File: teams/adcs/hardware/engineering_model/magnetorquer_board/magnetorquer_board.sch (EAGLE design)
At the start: 36 parts

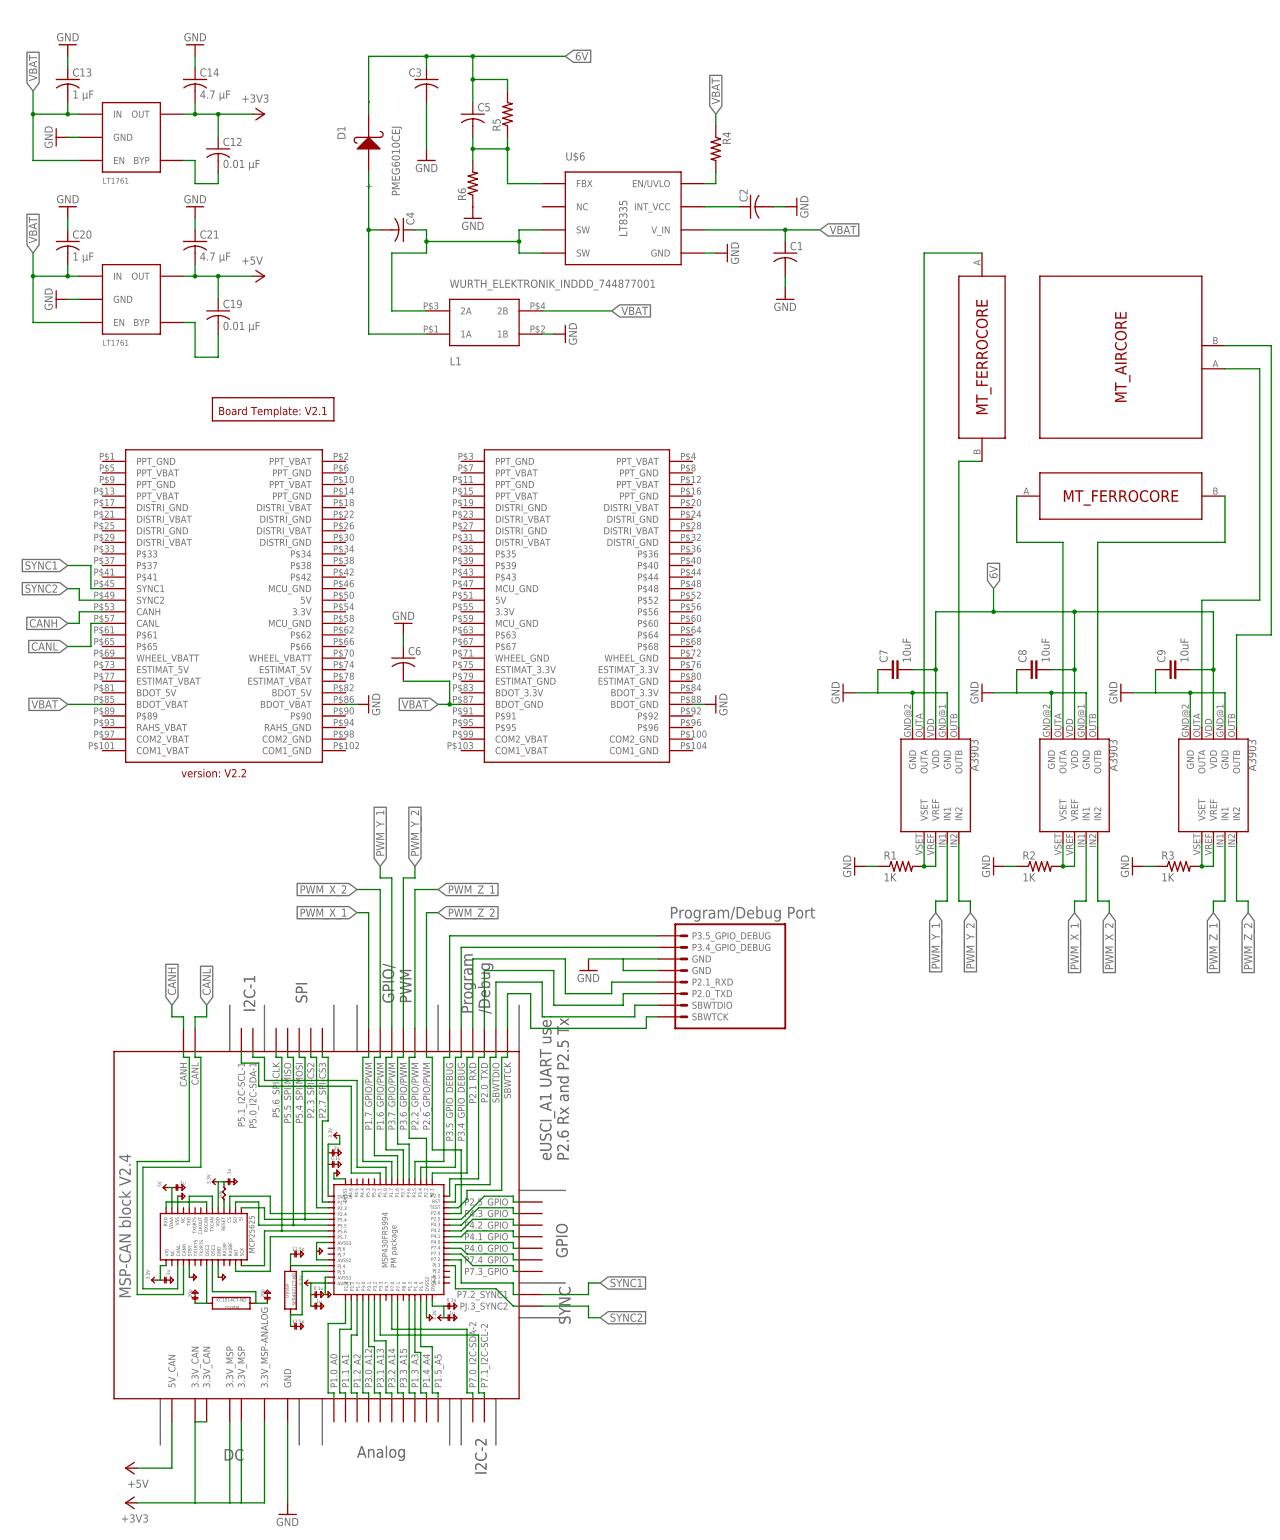
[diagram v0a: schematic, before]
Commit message: added two new capacitors to eagle library moved estimator, photodiode_center, and magetorquer board to their own foldr and created gerbers for them
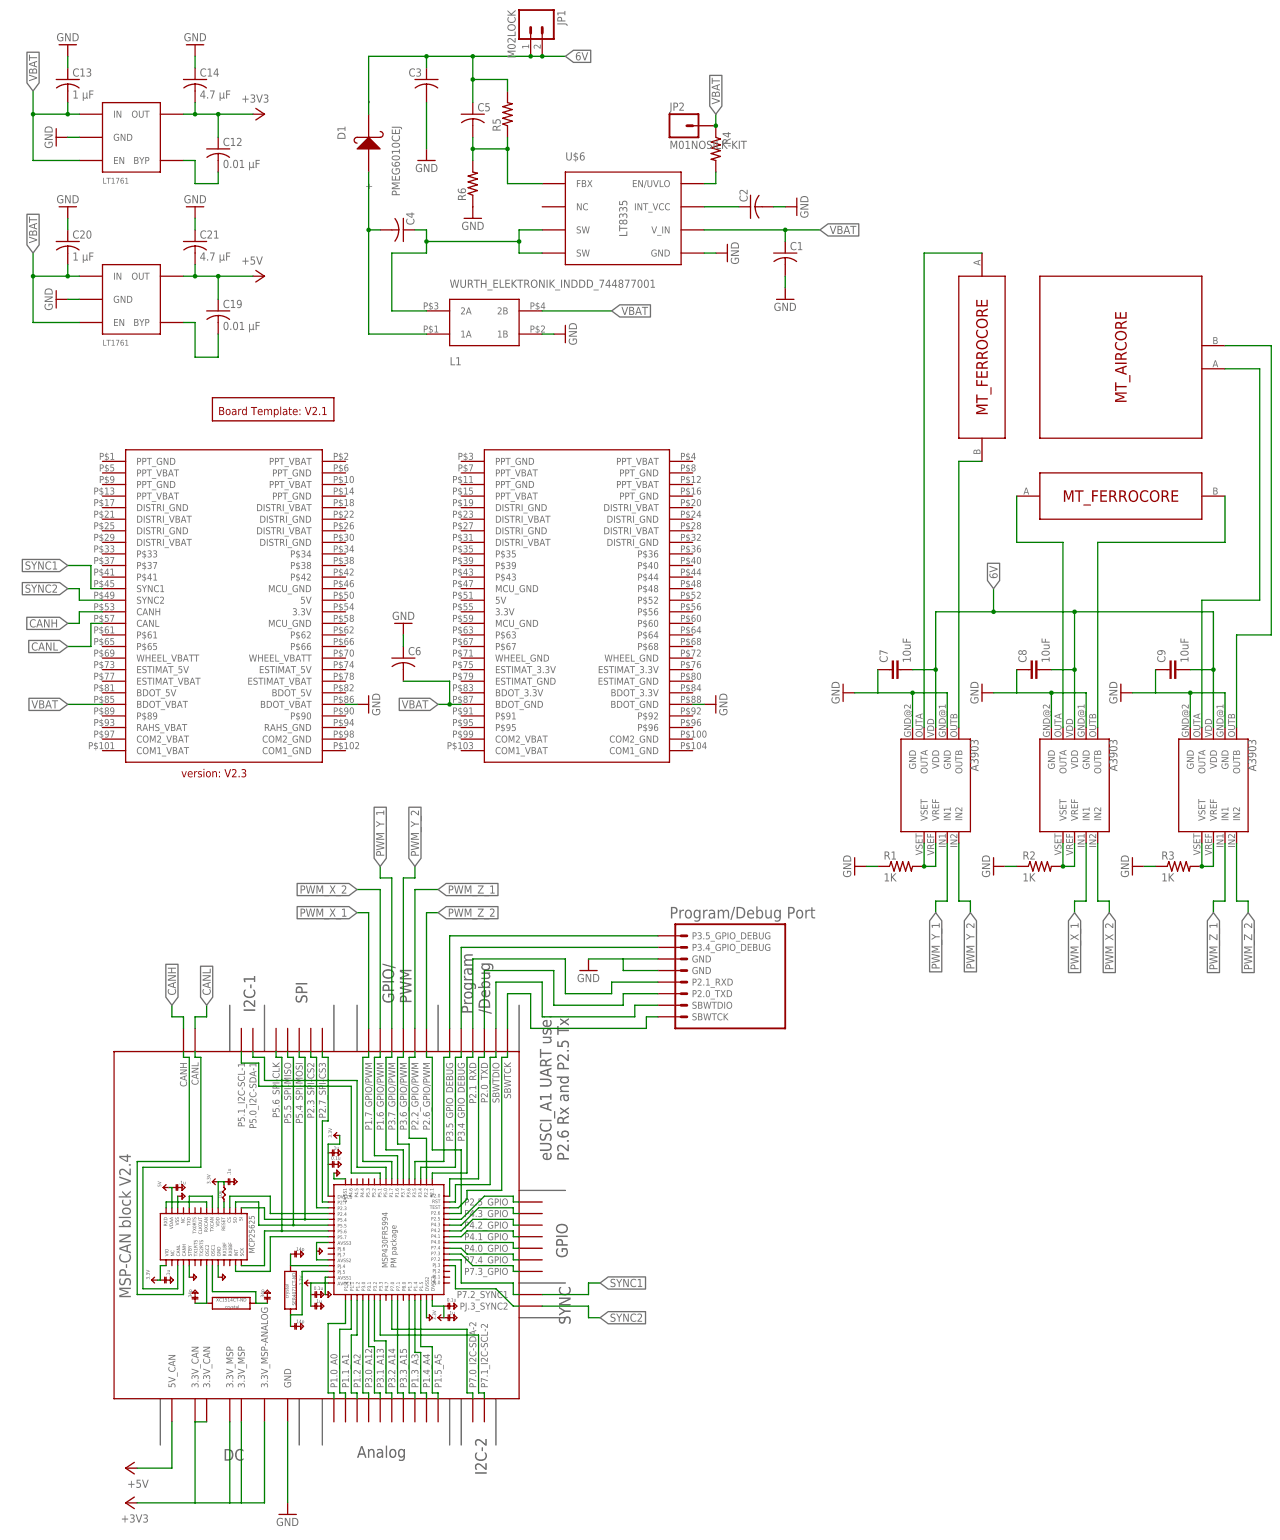
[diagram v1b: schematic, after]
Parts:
- added JP1: M02LOCK, SparkFun-Connectors:M02LOCK
- added JP2: M01NOSILK-KIT, SparkFun-Connectors:M01NOSILK-KIT
- U$2: value BOARD_TEMPLATE -> BOARD_TEMPLATE1; device DubSat1 Components:BOARD_TEMPLATE -> DubSat1 Components:BOARD_TEMPLATE1
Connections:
- net 6V: now also JP1.1, JP1.2
- net VBAT: now also JP2.1
